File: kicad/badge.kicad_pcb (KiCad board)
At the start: 2 copper layers, 76.2 x 113 mm, 37 parts, among them U1 ATtiny85-20P, U2 4021, U3 74HC595, U4 74HC595

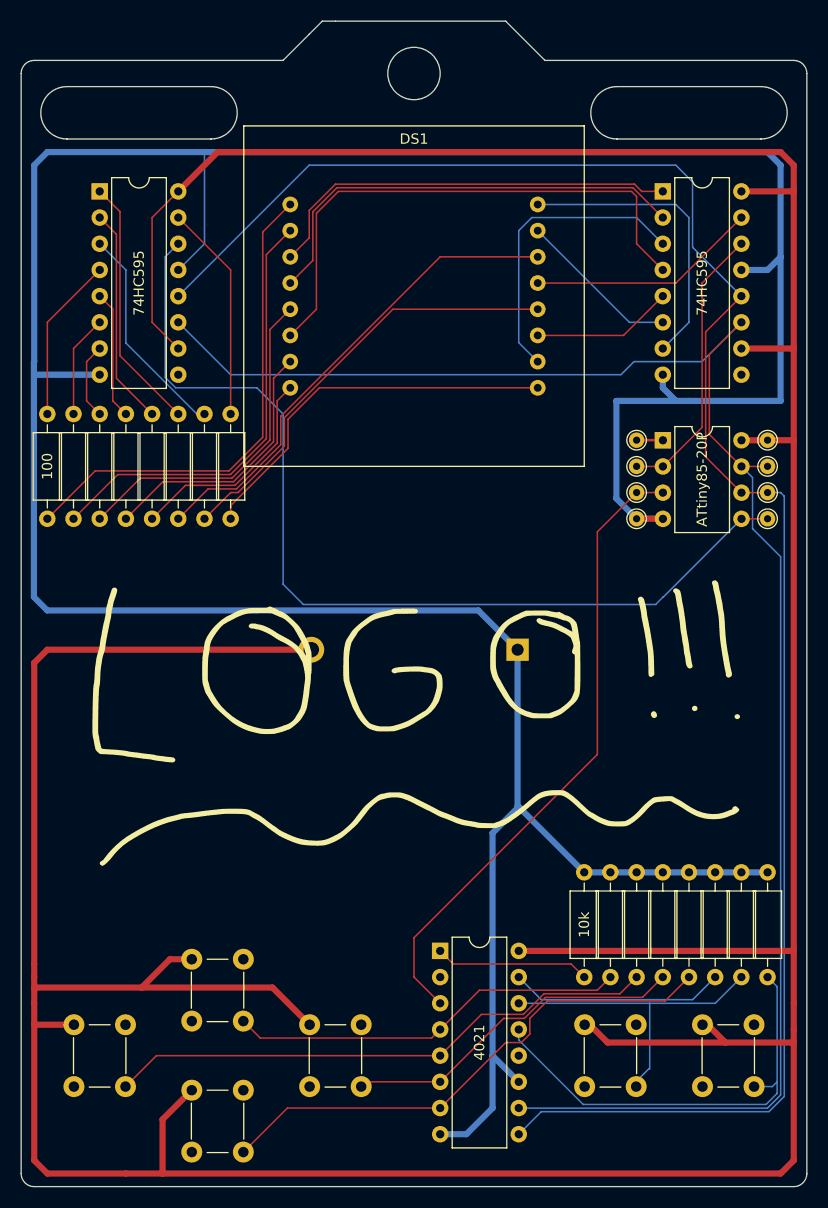
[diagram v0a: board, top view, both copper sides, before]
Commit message: Add surface mount parts
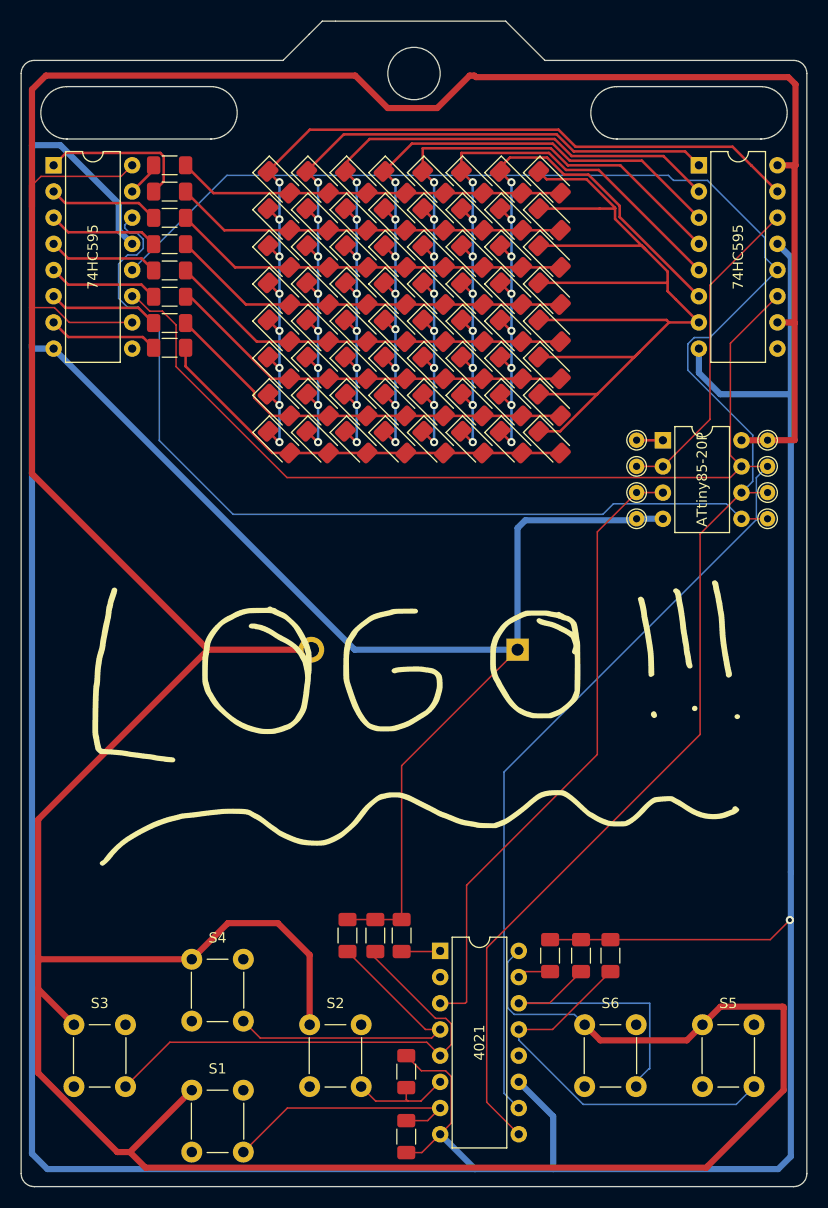
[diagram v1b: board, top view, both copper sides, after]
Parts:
- removed DS1: ~, badge:8x8 LED Matrix
- added D1: LED, LED_SMD:LED_1206_3216Metric_Pad1.42x1.75mm_HandSolder, F.Cu at (177.4, 42.3)
- added D10: LED, LED_SMD:LED_1206_3216Metric_Pad1.42x1.75mm_HandSolder, F.Cu at (181.1, 45.9)
- added D11: LED, LED_SMD:LED_1206_3216Metric_Pad1.42x1.75mm_HandSolder, F.Cu at (181.1, 49.5)
- added D12: LED, LED_SMD:LED_1206_3216Metric_Pad1.42x1.75mm_HandSolder, F.Cu at (181.1, 53.1)
- added D13: LED, LED_SMD:LED_1206_3216Metric_Pad1.42x1.75mm_HandSolder, F.Cu at (181.2, 56.7)
- added D14: LED, LED_SMD:LED_1206_3216Metric_Pad1.42x1.75mm_HandSolder, F.Cu at (181.2, 60.3)
- added D15: LED, LED_SMD:LED_1206_3216Metric_Pad1.42x1.75mm_HandSolder, F.Cu at (181.2, 63.9)
- added D16: LED, LED_SMD:LED_1206_3216Metric_Pad1.42x1.75mm_HandSolder, F.Cu at (181.2, 67.5)
- added D17: LED, LED_SMD:LED_1206_3216Metric_Pad1.42x1.75mm_HandSolder, F.Cu at (184.9, 42.3)
- added D18: LED, LED_SMD:LED_1206_3216Metric_Pad1.42x1.75mm_HandSolder, F.Cu at (184.9, 45.9)
- added D19: LED, LED_SMD:LED_1206_3216Metric_Pad1.42x1.75mm_HandSolder, F.Cu at (184.9, 49.5)
- added D2: LED, LED_SMD:LED_1206_3216Metric_Pad1.42x1.75mm_HandSolder, F.Cu at (177.4, 45.9)
- added D20: LED, LED_SMD:LED_1206_3216Metric_Pad1.42x1.75mm_HandSolder, F.Cu at (184.9, 53.1)
- added D21: LED, LED_SMD:LED_1206_3216Metric_Pad1.42x1.75mm_HandSolder, F.Cu at (184.9, 56.7)
- added D22: LED, LED_SMD:LED_1206_3216Metric_Pad1.42x1.75mm_HandSolder, F.Cu at (184.9, 60.3)
- added D23: LED, LED_SMD:LED_1206_3216Metric_Pad1.42x1.75mm_HandSolder, F.Cu at (184.9, 63.9)
- added D24: LED, LED_SMD:LED_1206_3216Metric_Pad1.42x1.75mm_HandSolder, F.Cu at (184.9, 67.5)
- added D25: LED, LED_SMD:LED_1206_3216Metric_Pad1.42x1.75mm_HandSolder, F.Cu at (188.7, 42.3)
- added D26: LED, LED_SMD:LED_1206_3216Metric_Pad1.42x1.75mm_HandSolder, F.Cu at (188.7, 45.9)
- added D27: LED, LED_SMD:LED_1206_3216Metric_Pad1.42x1.75mm_HandSolder, F.Cu at (188.7, 49.5)
- added D28: LED, LED_SMD:LED_1206_3216Metric_Pad1.42x1.75mm_HandSolder, F.Cu at (188.7, 53.1)
- added D29: LED, LED_SMD:LED_1206_3216Metric_Pad1.42x1.75mm_HandSolder, F.Cu at (188.7, 56.7)
- added D3: LED, LED_SMD:LED_1206_3216Metric_Pad1.42x1.75mm_HandSolder, F.Cu at (177.4, 49.5)
- added D30: LED, LED_SMD:LED_1206_3216Metric_Pad1.42x1.75mm_HandSolder, F.Cu at (188.7, 60.3)
- added D31: LED, LED_SMD:LED_1206_3216Metric_Pad1.42x1.75mm_HandSolder, F.Cu at (188.7, 63.9)
- added D32: LED, LED_SMD:LED_1206_3216Metric_Pad1.42x1.75mm_HandSolder, F.Cu at (188.7, 67.5)
- added D33: LED, LED_SMD:LED_1206_3216Metric_Pad1.42x1.75mm_HandSolder, F.Cu at (192.4, 42.3)
- added D34: LED, LED_SMD:LED_1206_3216Metric_Pad1.42x1.75mm_HandSolder, F.Cu at (192.4, 45.9)
- added D35: LED, LED_SMD:LED_1206_3216Metric_Pad1.42x1.75mm_HandSolder, F.Cu at (192.4, 49.5)
- added D36: LED, LED_SMD:LED_1206_3216Metric_Pad1.42x1.75mm_HandSolder, F.Cu at (192.4, 53.1)
- added D37: LED, LED_SMD:LED_1206_3216Metric_Pad1.42x1.75mm_HandSolder, F.Cu at (192.4, 56.7)
- added D38: LED, LED_SMD:LED_1206_3216Metric_Pad1.42x1.75mm_HandSolder, F.Cu at (192.4, 60.3)
- added D39: LED, LED_SMD:LED_1206_3216Metric_Pad1.42x1.75mm_HandSolder, F.Cu at (192.4, 63.9)
- added D4: LED, LED_SMD:LED_1206_3216Metric_Pad1.42x1.75mm_HandSolder, F.Cu at (177.4, 53.1)
- added D40: LED, LED_SMD:LED_1206_3216Metric_Pad1.42x1.75mm_HandSolder, F.Cu at (192.4, 67.5)
- added D41: LED, LED_SMD:LED_1206_3216Metric_Pad1.42x1.75mm_HandSolder, F.Cu at (196.2, 42.3)
- added D42: LED, LED_SMD:LED_1206_3216Metric_Pad1.42x1.75mm_HandSolder, F.Cu at (196.2, 45.9)
- added D43: LED, LED_SMD:LED_1206_3216Metric_Pad1.42x1.75mm_HandSolder, F.Cu at (196.2, 49.5)
- added D44: LED, LED_SMD:LED_1206_3216Metric_Pad1.42x1.75mm_HandSolder, F.Cu at (196.2, 53.1)
- added D45: LED, LED_SMD:LED_1206_3216Metric_Pad1.42x1.75mm_HandSolder, F.Cu at (196.2, 56.7)
- added D46: LED, LED_SMD:LED_1206_3216Metric_Pad1.42x1.75mm_HandSolder, F.Cu at (196.2, 60.3)
- added D47: LED, LED_SMD:LED_1206_3216Metric_Pad1.42x1.75mm_HandSolder, F.Cu at (196.2, 63.9)
- added D48: LED, LED_SMD:LED_1206_3216Metric_Pad1.42x1.75mm_HandSolder, F.Cu at (196.2, 67.5)
- added D49: LED, LED_SMD:LED_1206_3216Metric_Pad1.42x1.75mm_HandSolder, F.Cu at (199.9, 42.3)
- added D5: LED, LED_SMD:LED_1206_3216Metric_Pad1.42x1.75mm_HandSolder, F.Cu at (177.4, 56.7)
- added D50: LED, LED_SMD:LED_1206_3216Metric_Pad1.42x1.75mm_HandSolder, F.Cu at (199.9, 45.9)
- added D51: LED, LED_SMD:LED_1206_3216Metric_Pad1.42x1.75mm_HandSolder, F.Cu at (199.9, 49.5)
- added D52: LED, LED_SMD:LED_1206_3216Metric_Pad1.42x1.75mm_HandSolder, F.Cu at (199.9, 53.1)
- added D53: LED, LED_SMD:LED_1206_3216Metric_Pad1.42x1.75mm_HandSolder, F.Cu at (199.9, 56.7)
- added D54: LED, LED_SMD:LED_1206_3216Metric_Pad1.42x1.75mm_HandSolder, F.Cu at (199.9, 60.3)
- added D55: LED, LED_SMD:LED_1206_3216Metric_Pad1.42x1.75mm_HandSolder, F.Cu at (199.9, 63.9)
- added D56: LED, LED_SMD:LED_1206_3216Metric_Pad1.42x1.75mm_HandSolder, F.Cu at (199.9, 67.5)
- added D57: LED, LED_SMD:LED_1206_3216Metric_Pad1.42x1.75mm_HandSolder, F.Cu at (203.7, 42.3)
- added D58: LED, LED_SMD:LED_1206_3216Metric_Pad1.42x1.75mm_HandSolder, F.Cu at (203.7, 45.9)
- added D59: LED, LED_SMD:LED_1206_3216Metric_Pad1.42x1.75mm_HandSolder, F.Cu at (203.7, 49.5)
- added D6: LED, LED_SMD:LED_1206_3216Metric_Pad1.42x1.75mm_HandSolder, F.Cu at (177.4, 60.3)
- added D60: LED, LED_SMD:LED_1206_3216Metric_Pad1.42x1.75mm_HandSolder, F.Cu at (203.7, 53.1)
- added D61: LED, LED_SMD:LED_1206_3216Metric_Pad1.42x1.75mm_HandSolder, F.Cu at (203.7, 56.7)
- added D62: LED, LED_SMD:LED_1206_3216Metric_Pad1.42x1.75mm_HandSolder, F.Cu at (203.7, 60.3)
- added D63: LED, LED_SMD:LED_1206_3216Metric_Pad1.42x1.75mm_HandSolder, F.Cu at (203.7, 63.9)
- added D64: LED, LED_SMD:LED_1206_3216Metric_Pad1.42x1.75mm_HandSolder, F.Cu at (203.7, 67.5)
- added D7: LED, LED_SMD:LED_1206_3216Metric_Pad1.42x1.75mm_HandSolder, F.Cu at (177.4, 63.9)
- added D8: LED, LED_SMD:LED_1206_3216Metric_Pad1.42x1.75mm_HandSolder, F.Cu at (177.4, 67.5)
- added D9: LED, LED_SMD:LED_1206_3216Metric_Pad1.42x1.75mm_HandSolder, F.Cu at (181.1, 42.3)
- R1, R10, R11, R12, R13, R14, R15, R16, R2, R3, R4, R5, R6, R7, R8, R9: footprint Resistor_THT:R_Axial_DIN0207_L6.3mm_D2.5mm_P10.16mm_Horizontal -> Resistor_SMD:R_1206_3216Metric_Pad1.30x1.75mm_HandSolder
- S1, S2, S3, S4, S5, S6: footprint badge:button -> badge-footprints:button
- moved R16 31.5 mm to (189.8, 134.8), turned to -90 degrees
- moved R15 26.5 mm to (189.8, 128.6)
- moved R13 25.8 mm to (184.1, 115.3)
- moved R14 25.7 mm to (186.8, 115.3)
- moved R1 24.8 mm to (166.8, 40.6), turned to 0 degrees
- moved R2 21.6 mm to (166.8, 43.2), turned to 0 degrees
- moved R3 19.1 mm to (166.8, 45.8), turned to 0 degrees
- moved R5 18.3 mm to (166.8, 50.9), turned to 0 degrees
- moved R9 18.2 mm to (189.3, 115.3)
- moved R4 16.8 mm to (166.8, 48.3), turned to 0 degrees
- moved R10 16.1 mm to (203.7, 117.3)
- moved R11 15.7 mm to (206.7, 117.3)
- moved R12 15.4 mm to (209.6, 117.3)
- moved R7 12.8 mm to (166.8, 56.0), turned to 0 degrees
- moved R6 12.1 mm to (166.8, 53.4), turned to 0 degrees
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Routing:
- net GND: track 328.8 -> 465.1 mm, vias 0 -> 1
- net Net-(D57-K): track 28.9 -> 102.2 mm
- net Net-(D1-K): track 22.4 -> 91.5 mm, vias 0 -> 8
- net Net-(D41-K): track 13.7 -> 67.2 mm, vias 0 -> 8
- net Net-(D49-K): track 15.8 -> 64.1 mm, vias 0 -> 8
- net Net-(D25-K): track 29.0 -> 72.7 mm, vias 0 -> 8
- net Net-(D10-K): track 40.9 -> 79.0 mm, vias 0 -> 8
- net Net-(D17-K): track 43.9 -> 75.8 mm, vias 0 -> 8
- net Net-(U2-D0): track 51.1 -> 24.7 mm
- net Net-(U2-D1): track 35.0 -> 11.7 mm
- net Net-(U4-QA): track 21.2 -> 3.40 mm
- net Net-(U2-D6): track 20.9 -> 3.26 mm
- net Net-(D33-K): track 53.2 -> 70.7 mm, vias 0 -> 8
- net Net-(D11-A): track 21.1 -> 38.3 mm
- net Net-(D14-A): track 25.9 -> 39.6 mm
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
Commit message: Update surface mount badge
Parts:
- removed G***: LOGO, badge:logo
- BAT1: value BS-7 -> CR2032; footprint digikey-footprints:Battery_Holder_Coin_2032_BS-7 -> Battery:BatteryHolder_MPD_BC2003_1x2032; moved to F.Cu
- R1, R10, R11, R12, R13, R14, R15, R16, R2, R3, R4, R5, R6, R7, R8, R9: footprint Resistor_SMD:R_1206_3216Metric_Pad1.30x1.75mm_HandSolder -> PCM_JLCPCB:R_0805
- S1: value TL3315NF160Q -> C83206; footprint badge-footprints:button -> Button_Switch_SMD:SW_MEC_5GSH9
- S2, S3, S4, S5, S6: value TL3315NF160Q -> C83206; footprint badge-footprints:button -> Badge-Library:C83206
- U1: value ATtiny85-20P -> ATtiny85-20SF; footprint Package_DIP:DIP-8_W7.62mm -> Package_SO:SOIC-8_5.3x5.3mm_P1.27mm
- U2: value 4021 -> CD4021B; footprint Package_DIP:DIP-16_W7.62mm -> PCM_JLCPCB:SOIC-16_L9.9-W3.9-P1.27-LS6.0-BL
- U3, U4: value 74HC595 -> SN74HC595; footprint Package_DIP:DIP-16_W7.62mm -> PCM_JLCPCB:SOIC-16_L9.9-W3.9-P1.27-LS6.0-BL
- moved U2 61.5 mm to (163.6, 62.9), turned to -90 degrees
- moved R16 49.0 mm to (208.4, 89.5), turned to 0 degrees
- moved R15 40.9 mm to (208.4, 92.1), turned to 0 degrees
- moved R14 37.7 mm to (208.4, 84.5), turned to 0 degrees
- moved R13 37.4 mm to (208.4, 87.0), turned to 0 degrees
- moved TP2 36.6 mm to (224.8, 104.1)
- moved TP3 36.6 mm to (224.8, 106.7)
- moved TP1 36.6 mm to (224.8, 101.6)
- moved TP4 36.6 mm to (224.8, 109.2)
- moved R9 28.2 mm to (208.4, 94.6), turned to 0 degrees
- moved TP6 21.6 mm to (224.8, 94.0)
- moved TP7 21.6 mm to (224.8, 91.4)
- moved TP8 21.6 mm to (224.8, 88.9)
- moved TP5 21.6 mm to (224.8, 96.5)
- moved R10 20.7 mm to (208.4, 97.2), turned to 0 degrees
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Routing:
- net GND: track 465.1 -> 197.2 mm, vias 1 -> 3
- net Net-(U2-D1): track 11.7 -> 108.4 mm, vias 0 -> 2
- net Net-(U2-D5): track 28.9 -> 123.0 mm, vias 0 -> 2
- net Net-(U2-D0): track 24.7 -> 116.5 mm, vias 0 -> 2
- net Net-(U2-D6): track 3.26 -> 92.6 mm, vias 0 -> 2
- net Net-(U2-D7): track 3.76 -> 90.9 mm, vias 0 -> 2
- net Net-(U2-D4): track 38.4 -> 125.4 mm, vias 0 -> 2
- net Net-(U2-D3): track 32.2 -> 108.4 mm, vias 0 -> 2
- net Net-(U2-D2): track 47.0 -> 118.9 mm, vias 0 -> 2
- net Net-(U1-XTAL2/PB4): track 61.4 -> 119.3 mm, vias 0 -> 2
- net Net-(U1-~{RESET}/PB5): track 2.55 -> 48.3 mm
- net Net-(U1-PB1): track 176.7 -> 132.2 mm, vias 0 -> 3
- net Net-(U1-PB2): track 164.0 -> 124.7 mm, vias 0 -> 3
- net Net-(U1-XTAL1/PB3): track 31.3 -> 68.7 mm
- net Net-(D57-K): track 102.2 -> 70.8 mm
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
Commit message: Update badge
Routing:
- net Net-(U1-PB2): track 124.7 -> 123.2 mm
- net Net-(U1-AREF/PB0): track 106.2 -> 106.7 mm

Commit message: Update labels
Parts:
- moved R1 41.7 mm to (203.2, 72.7), turned to 90 degrees
- moved R2 36.7 mm to (199.6, 72.6), turned to 90 degrees
- moved R3 31.5 mm to (196.0, 72.6), turned to 90 degrees
- moved R4 26.5 mm to (192.5, 72.6), turned to 90 degrees
- moved D57 25.9 mm to (203.1, 68.2), turned to -135 degrees
- moved D64 25.8 mm to (177.9, 68.2), turned to -135 degrees
- moved D1 25.7 mm to (203.1, 42.0), turned to -135 degrees
- moved D8 25.5 mm to (177.9, 42.0), turned to -135 degrees
- moved D58 22.7 mm to (199.5, 68.2), turned to -135 degrees
- moved D63 22.6 mm to (181.5, 68.2), turned to -135 degrees
- moved D2 22.4 mm to (199.5, 42.0), turned to -135 degrees
- moved D49 22.4 mm to (203.1, 64.5), turned to -135 degrees
- moved D7 22.3 mm to (181.5, 42.0), turned to -135 degrees
- moved D9 22.2 mm to (203.1, 45.7), turned to -135 degrees
- moved D56 22.2 mm to (177.9, 64.5), turned to -135 degrees
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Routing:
- net Net-(U4-QA): track 25.6 -> 91.0 mm
- net Net-(U4-QB): track 25.0 -> 78.5 mm
- net Net-(U4-QC): track 20.7 -> 72.6 mm
- net Net-(U4-QD): track 18.0 -> 66.7 mm
- net Net-(U4-QE): track 18.5 -> 60.0 mm
- net Net-(U4-QF): track 19.5 -> 54.3 mm
- net Net-(D1-K): track 87.6 -> 55.3 mm
- net Net-(D10-K): track 77.8 -> 49.7 mm
- net Net-(U4-QG): track 22.3 -> 47.8 mm
- net Net-(D17-K): track 73.6 -> 51.6 mm
- net Net-(U4-QH): track 24.1 -> 42.1 mm
- net Net-(D25-K): track 70.4 -> 54.2 mm
- net VCC: track 406.2 -> 393.9 mm
- net Net-(D33-K): track 66.6 -> 56.4 mm
- net Net-(D57-K): track 70.8 -> 62.2 mm, vias 0 -> 8
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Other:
- board text added: "This badge is hackable github.com/joshbressers/badge"

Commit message: Update badge
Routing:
- net Net-(U2-D5): track 123.0 -> 121.5 mm
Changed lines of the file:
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@@
 			(drillshape 0)
 			(scaleselection 1)
-			(outputdirectory "surface-gerber/")
+			(outputdirectory "20250921-output/20250921-gerber/")
 		)
 	)
@@
 		(tags "BC2003 CR2032 2032 Battery Holder")
 		(property "Reference" "BAT1"
-			(at -3.4036 -11.176 90)
+			(at -3.2004 -11.2268 90)
 			(layer "F.SilkS")
 			(effects
@@
 		)
 		(property "Value" "CR2032"
-			(at 0 11.2 90)
+			(at 0.002187 11.6332 90)
 			(layer "F.SilkS")
 			(effects
@@
 		(fp_line
 			(start 10.47 4.885)
-			(end 8.86291 4.885)
+			(end 8.862909 4.885)
 			(stroke
 				(width 0.12)
@@
 		)
 		(fp_line
-			(start -10.47 3)
+			(start 10.47 4.885)
+			(end 10.35 4.765)
+			(stroke
+				(width 0.12)
+				(type default)
+			)
+			(layer "F.SilkS")
+		)
+		(fp_line
+			(start -10.47 2.525)
 			(end -10.47 4.885)
 			(stroke
@@
 		)
 		(fp_line
-			(start 10.47 3)
+			(start 10.47 2.525)
 			(end 10.47 4.885)
 			(stroke
@@
 		)
 		(fp_line
-			(start -10.47 -3)
+			(start -10.47 -2.525)
 			(end -10.47 -4.885)
 			(stroke
@@
 		)
 		(fp_line
-			(start 10.47 -3)
+			(start 10.47 -2.525)
 			(end 10.47 -4.885)
 			(stroke
@@
 		(fp_line
 			(start -10.47 -4.885)
-			(end -8.86291 -4.885)
+			(end -8.862908 -4.885)
 			(stroke
 				(width 0.12)
@@
 		(fp_line
 			(start 10.47 -4.885)
-			(end 8.86291 -4.885)
+			(end 8.862908 -4.885)
 			(stroke
 				(width 0.12)
@@
 		)
 		(fp_arc
-			(start 8.865021 4.881168)
+			(start 8.862909 4.885)
 			(mid 0.002187 10.12)
 			(end -8.86291 4.885)
@@
 		)
 		(fp_arc
-			(start -8.86291 -4.885)
+			(start -8.862908 -4.885)
 			(mid 0 -10.12)
-			(end 8.86291 -4.885)
+			(end 8.862908 -4.885)
 			(stroke
 				(width 0.12)
@@
 		)
 		(fp_circle
-			(center 0 -11.2268)
-			(end 0.1524 -10.8712)
+			(center 0.8636 -11.0744)
+			(end 1.016 -10.7188)
 			(stroke
 				(width 0.1)
@@
 		(fp_line
 			(start -10.6 5.01)
-			(end -8.94 5.01)
+			(end -8.939999 5.01)
 			(stroke
 				(width 0.05)
@@
 		)
 		(fp_line
-			(start 8.94 5.01)
+			(start 8.939996 5.01)
 			(end 10.6 5.01)
 			(stroke
@@
 		)
 		(fp_line
-			(start -8.94 -5.01)
+			(start -8.939999 -5.01)
 			(end -10.6 -5.01)
 			(stroke
@@
 		)
 		(fp_line
-			(start 8.94 -5.01)
+			(start 8.939999 -5.01)
 			(end 10.6 -5.01)
 			(stroke
@@
 		)
 		(fp_arc
-			(start 8.92534 5.036071)
+			(start 8.939996 5.01)
 			(mid -0.014955 10.248096)
-			(end -8.94 5.01)
+			(end -8.939999 5.01)
 			(stroke
 				(width 0.05)
@@
 		)
 		(fp_arc
-			(start -8.934116 -5.020486)
+			(start -8.939999 -5.01)
 			(mid 0.006012 -10.248106)
-			(end 8.94 -5.01)
+			(end 8.939999 -5.01)
 			(stroke
 				(width 0.05)
@@
 		)
 		(fp_line
-			(start -10.35 2.525)
+			(start -10.47 2.525)
 			(end -12 2.525)
 			(stroke
@@
 		)
 		(fp_line
-			(start 10.35 2.525)
+			(start 10.47 2.525)
 			(end 12 2.525)
 			(stroke
@@
 		)
 		(fp_line
-			(start -10.35 -2.525)
+			(start -10.47 -2.525)
 			(end -12 -2.525)
 			(stroke
@@
 		)
 		(fp_line
-			(start 10.35 -2.525)
+			(start 10.47 -2.525)
 			(end 12 -2.525)
 			(stroke
@@
 		)
 		(fp_text user "-"
-			(at -1.9304 -6.9596 270)
+			(at -1.3208 -8.4328 270)
 			(unlocked yes)
 			(layer "F.SilkS")
@@
 		)
 		(fp_text user "+"
-			(at 11.1252 -3.4036 270)
+			(at 8.7376 -3 270)
 			(unlocked yes)
 			(layer "F.SilkS")
@@
 	)
 	(segment
-		(start 198.0275 109.1275)
-		(end 197.9005 109.2545)
-		(width 0.15)
-		(layer "F.Cu")
-		(net 4)
-	)
-	(segment
 		(start 159.888413 60.198)
 		(end 159.966413 60.276)
@@
 	)
 	(segment
-		(start 191.6775 115.4775)
-		(end 188.976 118.179)
+		(start 198.0275 109.1275)
+		(end 190.754 116.401)
 		(width 0.15)
 		(layer "F.Cu")
@@
 	)
 	(segment
-		(start 188.976 119.634)
+		(start 190.754 121.412)
 		(end 191.592 122.25)
 		(width 0.15)
@@
 	)
 	(segment
-		(start 157.48 60.96)
-		(end 158.242 60.198)
-		(width 0.15)
-		(layer "F.Cu")
-		(net 4)
-	)
-	(segment
-		(start 207.46 99.695)
-		(end 198.0275 109.1275)
+		(start 190.754 116.401)
+		(end 190.754 121.412)
 		(width 0.15)
 		(layer "F.Cu")
@@
 	)
 	(segment
-		(start 197.9005 109.2545)
-		(end 191.6775 115.4775)
+		(start 157.48 60.96)
+		(end 158.242 60.198)
 		(width 0.15)
 		(layer "F.Cu")
@@
 	)
 	(segment
-		(start 188.976 118.179)
-		(end 188.976 119.634)
+		(start 207.46 99.695)
+		(end 198.0275 109.1275)
 		(width 0.15)
 		(layer "F.Cu")
@@
 	)
 	(segment
-		(start 179.324 74.676)
-		(end 174.682328 74.676)
-		(width 0.15)
-		(layer "F.Cu")
-		(net 24)
-	)
-	(segment
 		(start 160.89 49.71)
 		(end 158.443 49.71)
@@
 	)
 	(segment
-		(start 179.324 74.676)
-		(end 180.975 74.676)
-		(width 0.15)
-		(layer "F.Cu")
-		(net 24)
-	)
-	(segment
 		(start 174.371 74.364672)
 		(end 174.682328 74.676)
@@
 	)
 	(segment
-		(start 179.345 74.676)
-		(end 179.324 74.676)
+		(start 169.40833 54.416)
+		(end 174.371 59.37867)
 		(width 0.15)
 		(layer "F.Cu")
@@
 	)
 	(segment
-		(start 169.40833 54.416)
-		(end 174.371 59.37867)
+		(start 181.61 74.041)
+		(end 181.61 73.554)
 		(width 0.15)
 		(layer "F.Cu")
@@
 	)
 	(segment
-		(start 181.61 74.041)
-		(end 181.61 73.554)
+		(start 180.975 74.676)
+		(end 174.682328 74.676)
 		(width 0.15)
 		(layer "F.Cu")
